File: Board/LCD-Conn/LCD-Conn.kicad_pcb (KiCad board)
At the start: 2 copper layers, 40 x 20 mm, 2 parts, among them J1 Conn_LCD, J2 Conn_Board

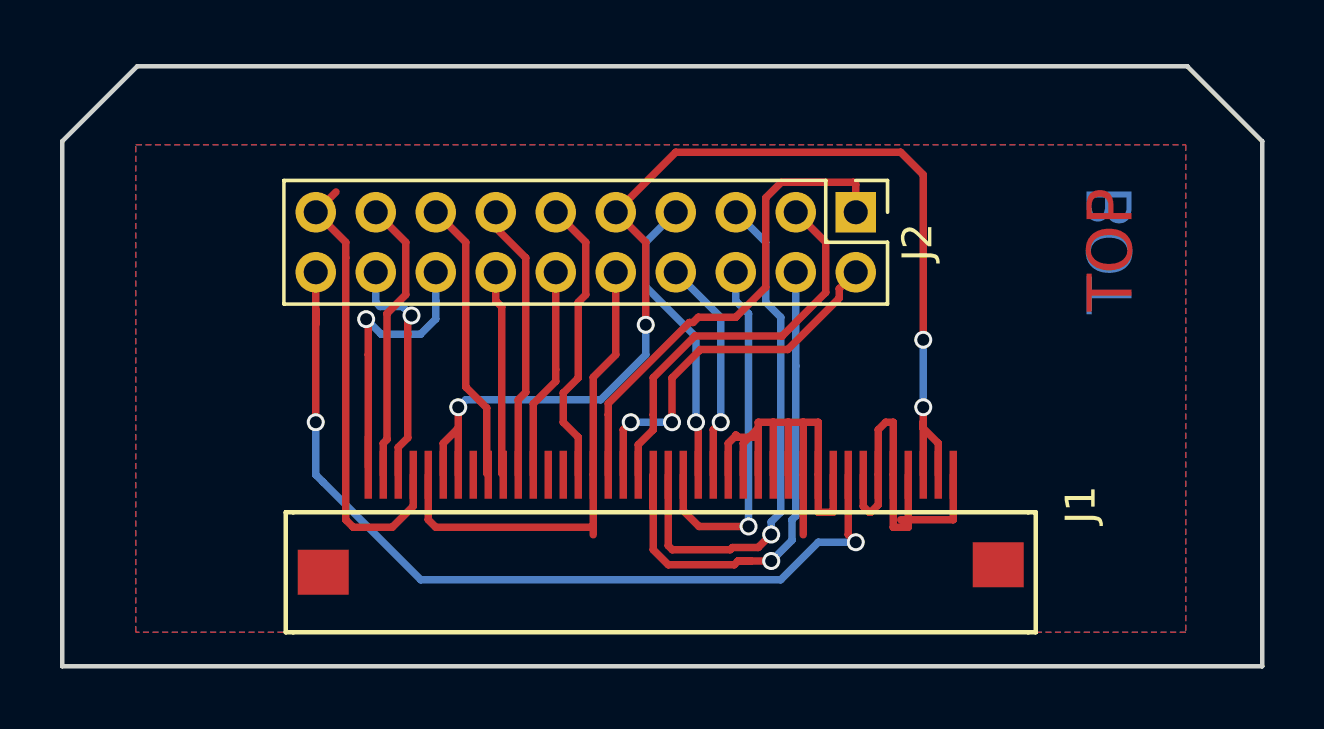
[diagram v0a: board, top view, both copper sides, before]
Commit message: Board: SD slot moved, usb-conn changed from slots to holes. LCD board polished. Repo cleaned up.
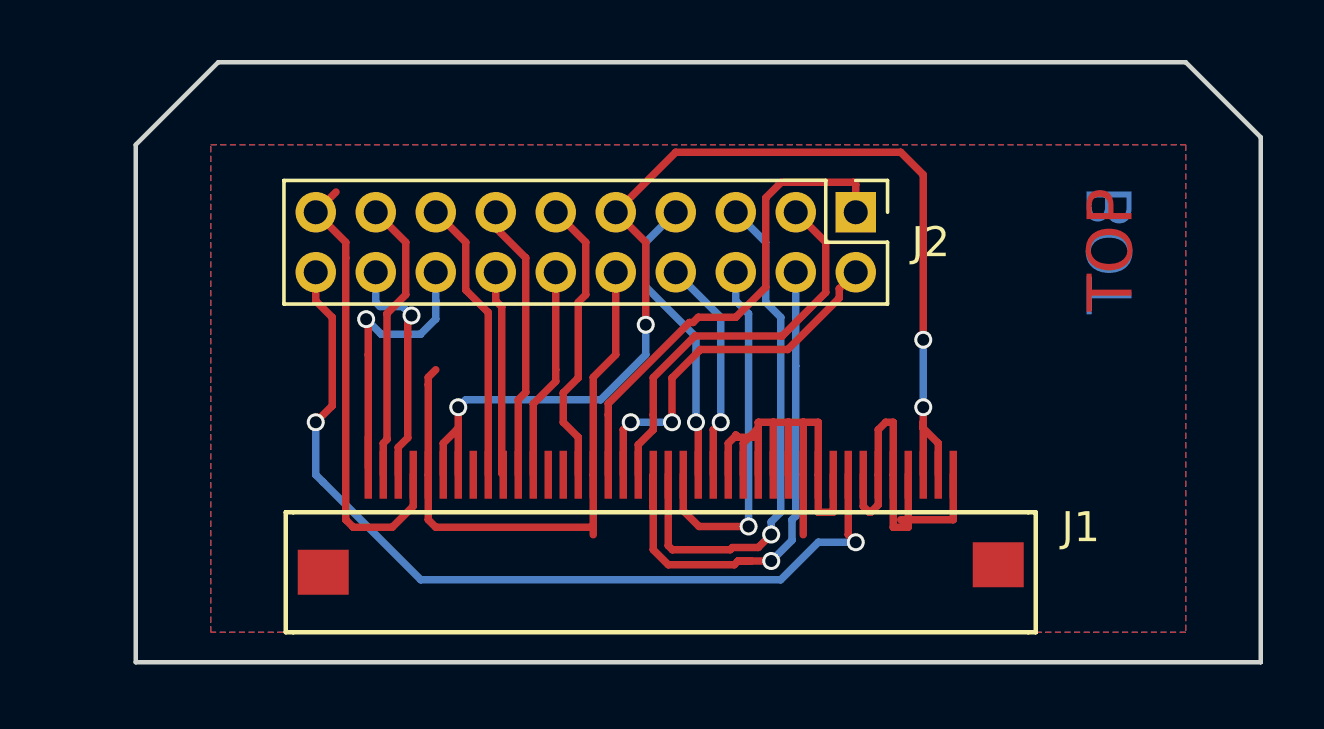
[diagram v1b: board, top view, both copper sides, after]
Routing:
- net GND: track 49.7 -> 53.3 mm
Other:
- board size 40 x 20 mm -> 37.5 x 20 mm
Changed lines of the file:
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@@
     (thickness 1.6)
     (drawings 8)
-    (tracks 221)
+    (tracks 224)
     (zones 0)
     (modules 2)
@@
   (module timekiller-footprints:LCD_conn (layer F.Cu)
     (at 185.75 111 90)
-    (fp_text reference J1 (at -1 23.25 90) (layer F.SilkS)
+    (fp_text reference J1 (at -1.75 23.25 180) (layer F.SilkS)
       (effects (font (size 1 1) (thickness 0.15)))
     )
-    (fp_text value Conn_LCD (at -0.25 -4.75 90) (layer F.Fab)
+    (fp_text value Conn_LCD (at -2.75 8.5 180) (layer F.Fab)
       (effects (font (size 1 1) (thickness 0.15)))
     )
@@
     (descr "Through hole straight pin header, 2x10, 2.00mm pitch, double rows")
     (tags "Through hole pin header THT 2x10 2.00mm double row")
-    (fp_text reference J2 (at 1 -2.06 270) (layer F.SilkS)
+    (fp_text reference J2 (at 1 -2.5 360) (layer F.SilkS)
       (effects (font (size 1 1) (thickness 0.15)))
     )
-    (fp_text value Conn_Board (at 1 20.06 270) (layer F.Fab)
+    (fp_text value Conn_Board (at -2.25 9.5 360) (layer F.Fab)
       (effects (font (size 1 1) (thickness 0.15)))
     )
@@
     (effects (font (size 1.5 1.5) (thickness 0.3)))
   )
-  (gr_line (start 215.05012 99.883964) (end 215.05012 117.383964) (layer Edge.Cuts) (width 0.15))
-  (gr_line (start 212.55012 97.383964) (end 215.05012 99.883964) (layer Edge.Cuts) (width 0.15))
-  (gr_line (start 177.55012 97.383964) (end 212.55012 97.383964) (layer Edge.Cuts) (width 0.15))
-  (gr_line (start 175.05012 99.883964) (end 177.55012 97.383964) (layer Edge.Cuts) (width 0.15))
-  (gr_line (start 175.05012 117.383964) (end 175.05012 99.883964) (layer Edge.Cuts) (width 0.15))
-  (gr_line (start 215.05012 117.383964) (end 175.05012 117.383964) (layer Edge.Cuts) (width 0.15))
+  (gr_line (start 215 99.75) (end 215 117.25) (layer Edge.Cuts) (width 0.15))
+  (gr_line (start 212.5 97.25) (end 215 99.75) (layer Edge.Cuts) (width 0.15))
+  (gr_line (start 180.25 97.25) (end 212.5 97.25) (layer Edge.Cuts) (width 0.15))
+  (gr_line (start 177.5 100) (end 180.25 97.25) (layer Edge.Cuts) (width 0.15))
+  (gr_line (start 177.5 117.25) (end 177.5 100) (layer Edge.Cuts) (width 0.15))
+  (gr_line (start 215 117.25) (end 177.5 117.25) (layer Edge.Cuts) (width 0.15))
   (segment (start 185.180054 105.813938) (end 185.683059 106.316943) (width 0.25) (layer B.Cu) (net 1))
   (segment (start 185.683059 106.316943) (end 186.991943 106.316943) (width 0.25) (layer B.Cu) (net 1))
@@
   (segment (start 184.500001 103.250001) (end 184.5 103.769998) (width 0.25) (layer F.Cu) (net 4))
   (segment (start 184.174999 101.575001) (end 183.5 102.25) (width 0.25) (layer F.Cu) (net 4))
+  (segment (start 187.25 107.75) (end 187.5 107.5) (width 0.25) (layer F.Cu) (net 5))
+  (segment (start 187.25 108) (end 187.25 107.75) (width 0.25) (layer F.Cu) (net 5))
+  (segment (start 187.25 111) (end 187.25 108) (width 0.25) (layer F.Cu) (net 5))
   (segment (start 200.25 109.25) (end 199.75 109.25) (width 0.25) (layer F.Cu) (net 5))
   (segment (start 200.25 111) (end 200.25 109.25) (width 0.25) (layer F.Cu) (net 5))
@@
   (segment (start 203.75 101) (end 203 100.25) (width 0.25) (layer F.Cu) (net 6))
   (segment (start 187.5 102.25) (end 188.5 103.25) (width 0.25) (layer F.Cu) (net 8))
-  (segment (start 188.5 103.25) (end 188.5 108.074998) (width 0.25) (layer F.Cu) (net 8))
-  (segment (start 188.5 108.074998) (end 189.200001 108.774999) (width 0.25) (layer F.Cu) (net 8))
-  (segment (start 189.200001 110.950001) (end 189.25 111) (width 0.25) (layer F.Cu) (net 8))
-  (segment (start 189.200001 108.774999) (end 189.200001 110.950001) (width 0.25) (layer F.Cu) (net 8))
+  (segment (start 188.5 103.25) (end 188.5 104.841004) (width 0.25) (layer F.Cu) (net 8))
+  (segment (start 188.5 104.841004) (end 189.25 105.591004) (width 0.25) (layer F.Cu) (net 8))
+  (segment (start 189.25 105.591004) (end 189.25 111) (width 0.25) (layer F.Cu) (net 8))
   (segment (start 189.5 104.25) (end 189.5 105.204594) (width 0.25) (layer F.Cu) (net 9))
   (segment (start 189.5 105.204594) (end 189.700001 105.404595) (width 0.25) (layer F.Cu) (net 9))
@@
   (segment (start 197 105.75) (end 197 109.25) (width 0.25) (layer B.Cu) (net 22))
   (via (at 197 109.25) (size 0.6) (drill 0.4) (layers F.Cu B.Cu) (net 22))
+  (segment (start 184.04999 105.754584) (end 184.04999 108.70001) (width 0.25) (layer F.Cu) (net 23))
+  (segment (start 184.04999 108.70001) (end 183.5 109.25) (width 0.25) (layer F.Cu) (net 23))
+  (segment (start 183.5 104.25) (end 183.5 105.204594) (width 0.25) (layer F.Cu) (net 23))
+  (segment (start 183.5 105.204594) (end 184.04999 105.754584) (width 0.25) (layer F.Cu) (net 23))
   (segment (start 187 114.5) (end 183.75 111.25) (width 0.25) (layer B.Cu) (net 23))
   (segment (start 183.5 111) (end 183.75 111.25) (width 0.25) (layer B.Cu) (net 23))
   (segment (start 183.5 109.25) (end 183.5 111) (width 0.25) (layer B.Cu) (net 23))
-  (segment (start 183.5 105.5) (end 183.5 106) (width 0.25) (layer F.Cu) (net 23))
-  (segment (start 183.5 104.25) (end 183.5 105.5) (width 0.25) (layer F.Cu) (net 23))
-  (segment (start 183.5 105.5) (end 183.5 109.25) (width 0.25) (layer F.Cu) (net 23))
   (via (at 183.5 109.25) (size 0.6) (drill 0.4) (layers F.Cu B.Cu) (net 23))
   (segment (start 201.5 113.25) (end 200.25 113.25) (width 0.25) (layer B.Cu) (net 23))
@@
     (polygon
       (pts
-        (xy 177.5 100) (xy 212.5 100) (xy 212.5 116.25) (xy 177.5 116.25)
+        (xy 180 100) (xy 212.5 100) (xy 212.5 116.25) (xy 180 116.25)
       )
     )
@@
     (polygon
       (pts
-        (xy 177.5 100) (xy 212.5 100) (xy 212.5 116.25) (xy 177.5 116.25)
+        (xy 180 100) (xy 212.5 100) (xy 212.5 116.25) (xy 180 116.25)
       )
     )

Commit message: pcbs polished a bit. Case bottom pcb clearance enlarged.
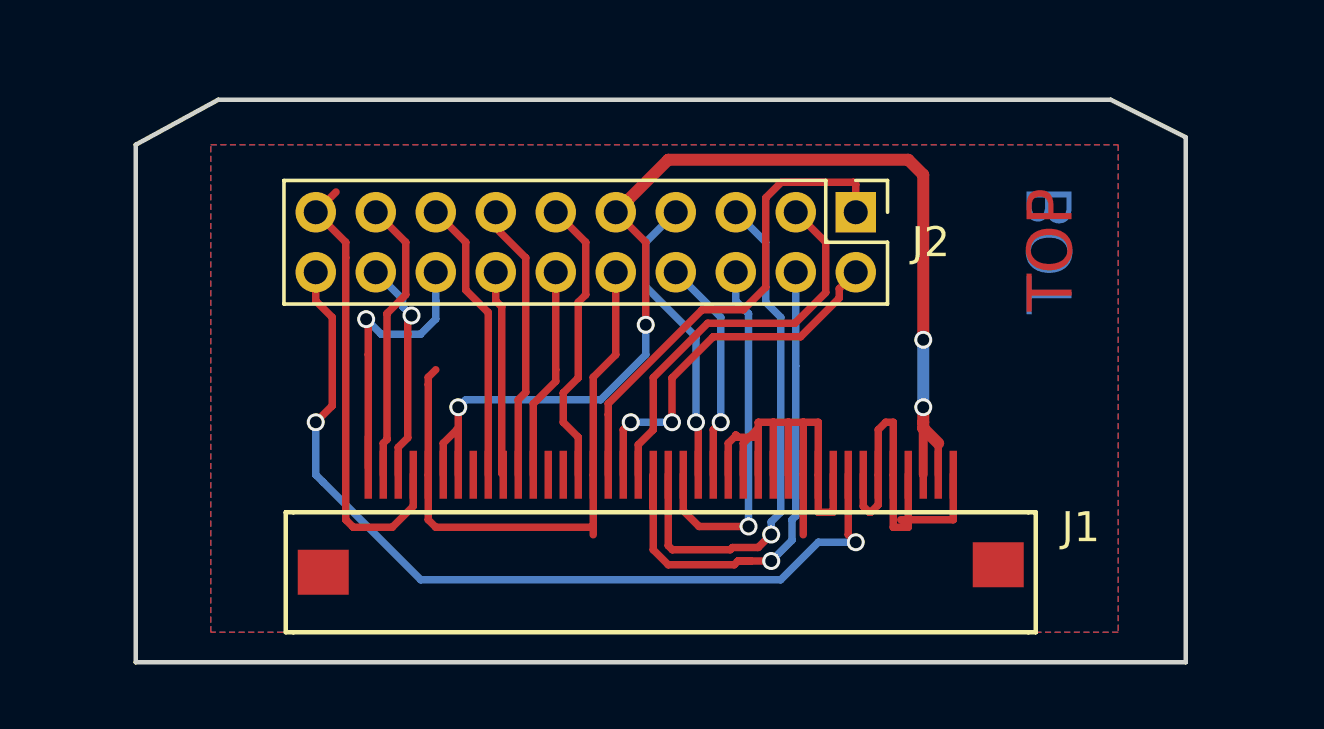
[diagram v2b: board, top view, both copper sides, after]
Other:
- board size 37.5 x 20 mm -> 35 x 18.8 mm

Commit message: system board polished, lcd flex connector footprint updated.
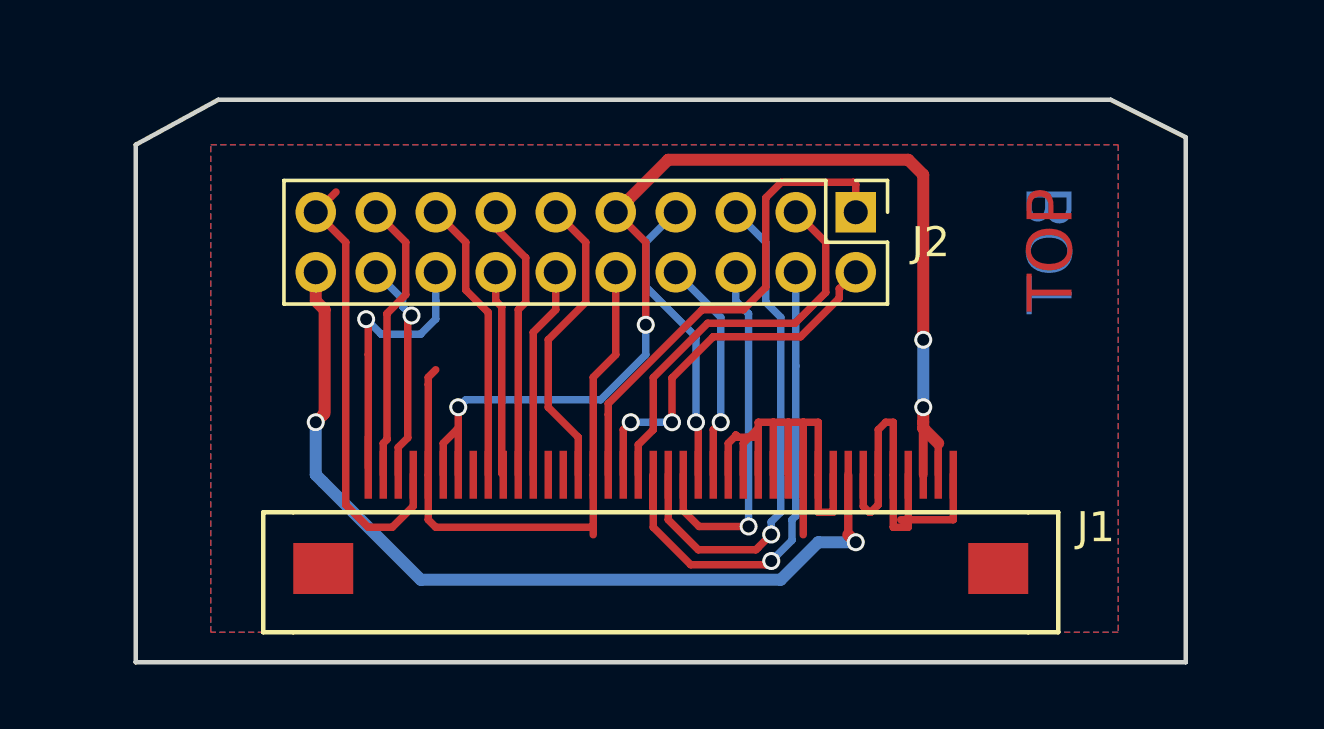
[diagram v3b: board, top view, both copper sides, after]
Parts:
- J1: footprint timekiller-footprints:LCD_conn -> LCD_conn
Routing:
- net LCD_D3: track 18.2 -> 17.3 mm
- net LCD_D4: track 17.6 -> 17.1 mm
